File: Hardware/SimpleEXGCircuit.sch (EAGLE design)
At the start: 27 parts

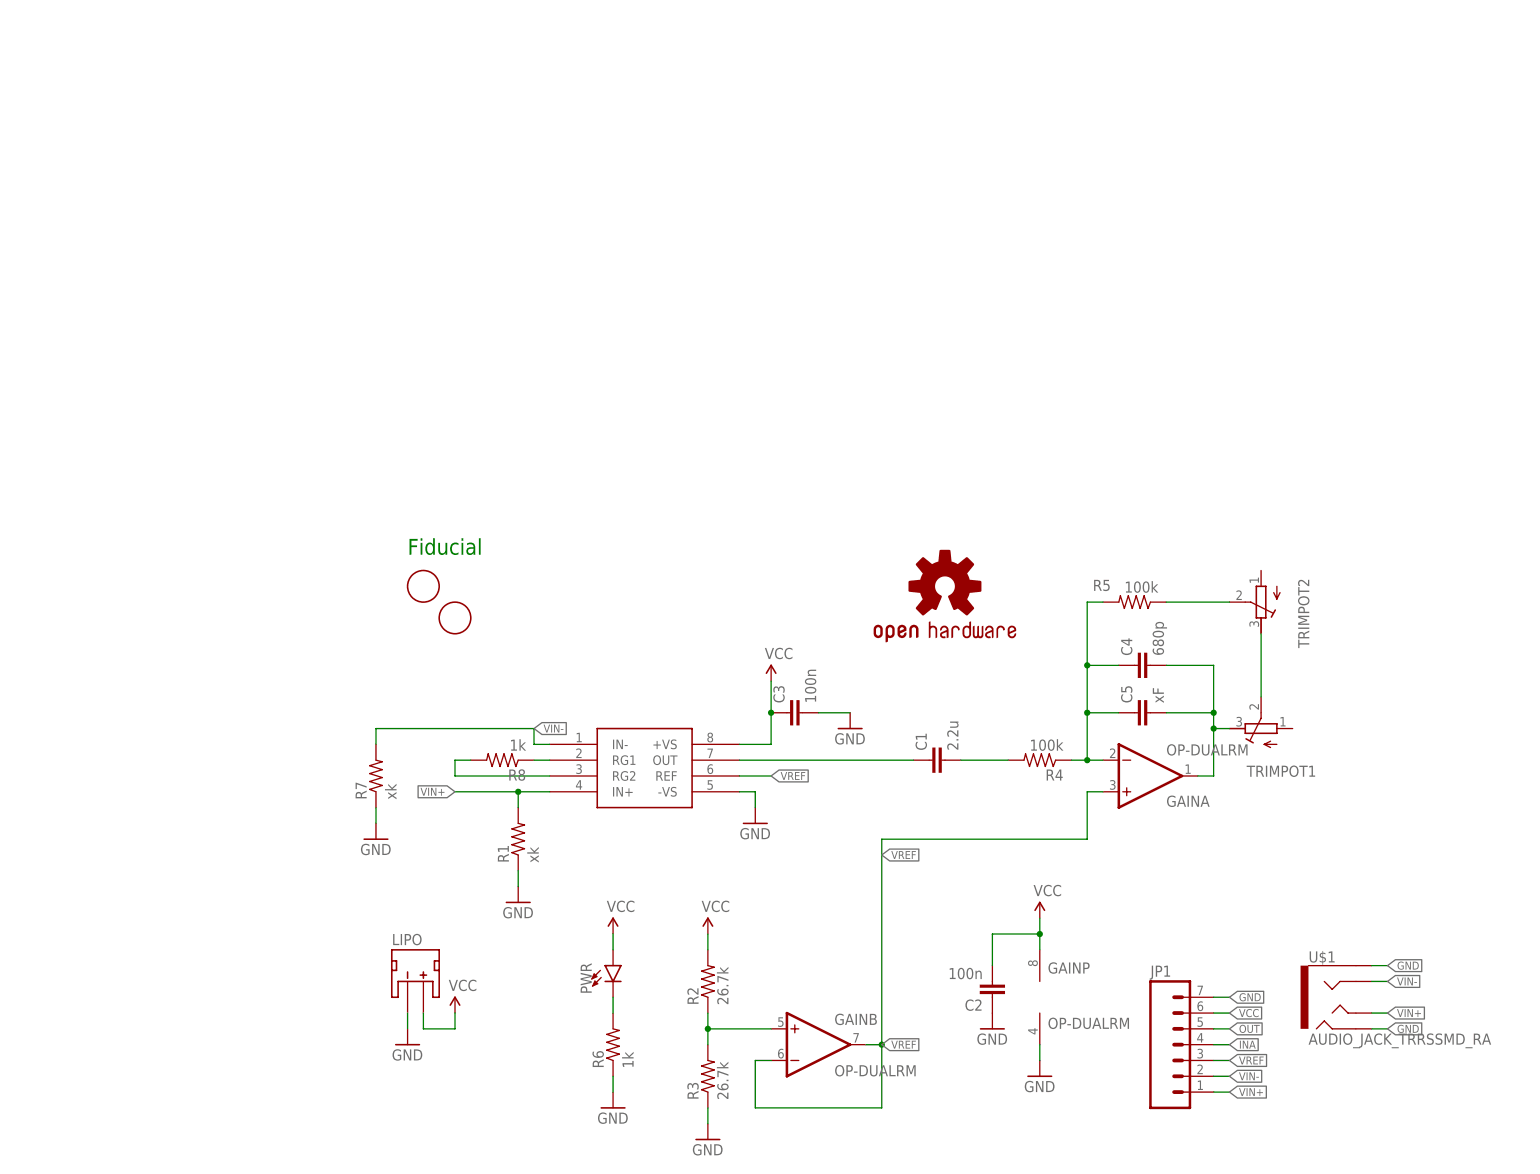
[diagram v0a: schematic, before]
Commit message: new hardware design with optoisolator and coin cell battery
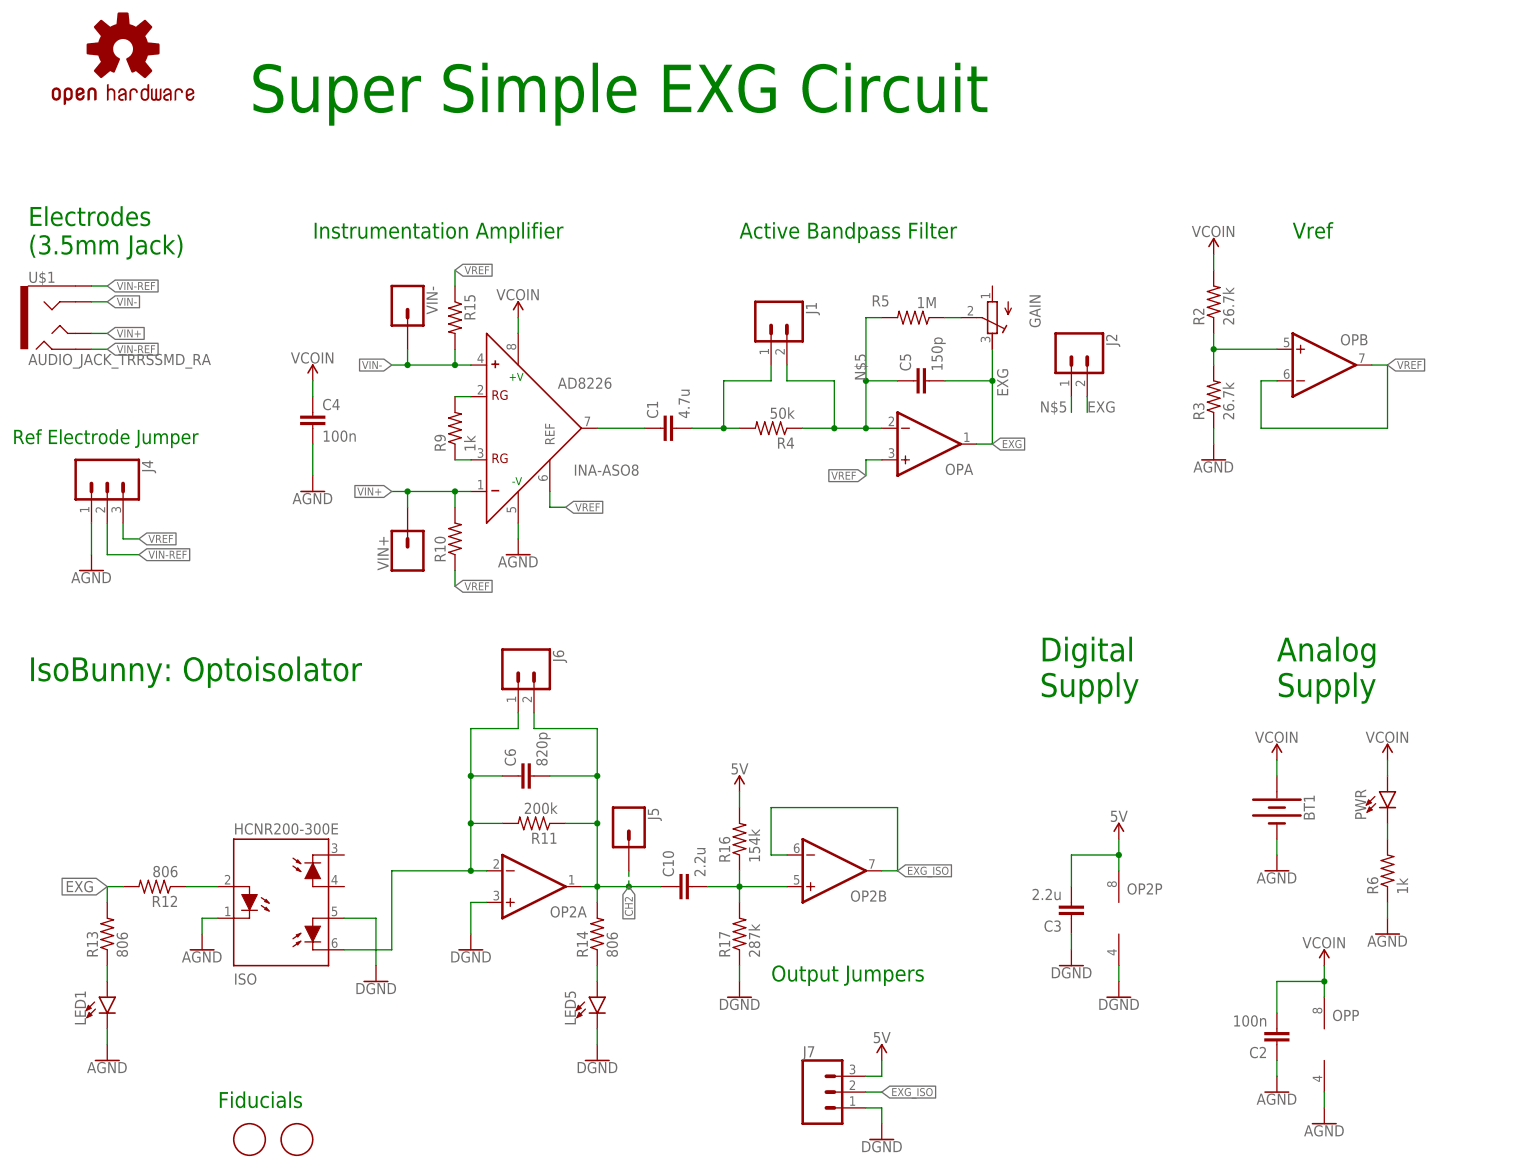
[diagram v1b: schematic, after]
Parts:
- removed INA: INA-B, CalvEngIO-AnalogIC:INA-B
- removed JP1: (no value), SparkFun-Connectors:M07
- removed LIPO: (no value), CalvEngIO-Connectors:JST_2MM_MALE
- removed R1, R7: xk, CalvEngIO-Passives:RESISTOR0402
- removed R8: 1k, CalvEngIO-Passives:RESISTOR0402
- removed TRIMPOT1, TRIMPOT2: (no value), CalvEngIO-Passives:TRIM-POT-P160
- removed U$2, U$3: FIDUCIAL, CalvEngIO-Connectors:FIDUCIAL
- added AD8226: INA-ASO8, CalvEngIO-AnalogIC:INA-ASO8
- added BT1: (no value), CalvEngIO-Connectors:BATTERY-20MM_SMD_4LEGS_OVERPASTE
- added C10: 2.2u, CalvEngIO-Passives:CAPACITOR0603
- added C6: 820p, CalvEngIO-Passives:CAPACITOR0603
- added ISO: HCNR200-300E, avago:HCNR200-300E
- added J1, J2, J6: (no value), CalvEngIO-Connectors:CONN_02
- added J4, J7: (no value), CalvEngIO-Connectors:CONN_03
- added J5: (no value), CalvEngIO-Connectors:CONN_01PTH_NO_SILK_KIT
- added LED1, LED5: (no value), CalvEngIO-LED:LED1206
- added LOGO4: OSHW-LOGOL, CalvEngIO-Logos:OSHW-LOGOL
- added OP, OP2: (no value), CalvEngIO-AnalogIC:OP-DUALR
- added R10, R15: (no value), CalvEngIO-Passives:RESISTOR0603
- added R11: 200k, CalvEngIO-Passives:RESISTOR0603
- added R12, R13, R14: 806, CalvEngIO-Passives:RESISTOR0603
- added R16: 154k, CalvEngIO-Passives:RESISTOR0603
- added R17: 287k, CalvEngIO-Passives:RESISTOR0603
- added R9: 1k, CalvEngIO-Passives:RESISTOR0603
- added VIN+, VIN-: (no value), CalvEngIO-Connectors:CONN_01
- C1: value 2.2u -> 4.7u
- C2: device CalvEngIO-Passives:CAPACITOR0402 -> CalvEngIO-Passives:CAPACITOR0603
- C3: value 100n -> 2.2u; device CalvEngIO-Passives:CAPACITOR0402 -> CalvEngIO-Passives:CAPACITOR0603
- C4: value 680p -> 100n; device CalvEngIO-Passives:CAPACITOR0402 -> CalvEngIO-Passives:CAPACITOR0603
- C5: value xF -> 150p; device resistor:C-EU025-024X044 -> CalvEngIO-Passives:CAPACITOR0603
- GAIN: value OP-DUALRM -> (none); device CalvEngIO-AnalogIC:OP-DUALRM -> CalvEngIO-Passives:TRIM-POT-P160
- LOGO1: value OSHW-LOGOS -> REVISION.C; device SparkFun-Aesthetics:OSHW-LOGOS -> CalvEngIO-Logos:REVISION.C
- PWR: device CalvEngIO-LED:LED0603 -> CalvEngIO-LED:LED1206
- R2, R3, R6: device CalvEngIO-Passives:RESISTOR0402 -> CalvEngIO-Passives:RESISTOR0603
- R4: value 100k -> 50k; device CalvEngIO-Passives:RESISTOR0402 -> CalvEngIO-Passives:RESISTOR0603
- R5: value 100k -> 1M; device CalvEngIO-Passives:RESISTOR0402 -> CalvEngIO-Passives:RESISTOR0603
- U$4: value WEBSITE.05 -> CALVENGIO_HANDLEHANDLE.05; device CalvEngIO-Logos:WEBSITE.05 -> CalvEngIO-Logos:CALVENGIO_HANDLEHANDLE.05
- U$5: value @HANDLE.1 -> FIDUCIAL; device CalvEngIO-Logos:@HANDLE.1 -> CalvEngIO-Connectors:FIDUCIAL
- U$6: value @HANDLE.05 -> FIDUCIAL; device CalvEngIO-Logos:@HANDLE.05 -> CalvEngIO-Connectors:FIDUCIAL
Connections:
- removed net GND: C2.1, C3.2, GAINP.V-, INA.-VS, JP1.7, LIPO.-, R1.1, R3.1, R6.1, R7.1, U$1.EARTH, U$1.RING2
- removed net N$4: C1.2, R4.2
- removed net OUT: C4.2, C5.2, GAINA.OUT, JP1.5, TRIMPOT1.E
- removed net VCC: C2.2, C3.1, GAINP.V+, INA.+VS, JP1.6, LIPO.+, PWR.A, R2.2
- new net 5V: C3.2, J7.3, OP2P.V+, R16.2
- new net AGND: AD8226.-V, BT1.-, C2.1, C4.2, ISO.C, J4.1, LED1.C, OPP.V-, R3.1, R6.1
- new net CH2: C10.1, C6.2, J5.1, J6.2, OP2A.OUT, R11.1, R14.2
- new net DGND: C3.1, ISO.A2, J7.1, LED5.C, OP2A.+IN, OP2P.V-, R17.1
- new net EXG: C5.2, GAIN.E, J2.2, OPA.OUT, R12.2, R13.2
- new net EXG_ISO: J7.2, OP2B.-IN, OP2B.OUT
- new net N$10: C6.1, ISO.C2, J6.1, OP2A.-IN, R11.2
- new net N$11: ISO.A, R12.1
- new net N$12: C10.2, OP2B.+IN, R16.1, R17.2
- new net N$17: LED1.A, R13.1
- new net N$19: LED5.A, R14.1
- new net VCOIN: AD8226.+V, BT1.+, C2.2, C4.1, OPP.V+, PWR.A, R2.2
- new net VIN-REF: J4.2, U$1.EARTH, U$1.RING2
- net INA: now also AD8226.OUT; no longer INA.OUT, JP1.4
- net N$1: now also GAIN.S; no longer TRIMPOT2.S
- net N$2: now also AD8226.RG@1, R9.2; no longer TRIMPOT1.S, TRIMPOT2.E
- net N$3: now also OPB.+IN; no longer GAINB.+IN
- net N$5: now also J1.2, J2.1, OPA.-IN; no longer C4.1, GAINA.-IN
- net N$7: now also AD8226.RG@2, R9.1; no longer INA.RG1, R8.1
- net N$8: now also C1.2, J1.1, R4.2; no longer INA.RG2, R8.2
- net VIN+: now also AD8226.IN-, R10.2, VIN+.1; no longer INA.IN+, JP1.1, R1.2
- net VIN-: now also AD8226.IN+, R15.2, VIN-.1; no longer INA.IN-, JP1.2, R7.2
- net VREF: now also AD8226.REF, J4.3, OPA.+IN, OPB.-IN, OPB.OUT, R10.1, R15.1; no longer GAINA.+IN, GAINB.-IN, GAINB.OUT, INA.REF, JP1.3
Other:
- note added: "Active Bandpass Filter"
- note added: "Analog Supply"
- note added: "Digital Supply"
- note added: "Electrodes (3.5mm Jack)"
- note added: "Fiducials"
- note added: "Instrumentation Amplifier"
- note added: "IsoBunny: Optoisolator"
- note added: "Output Jumpers"
- note added: "Ref Electrode Jumper"
- note added: "Super Simple EXG Circuit"
- note added: "Vref"
- note removed: "Creative Commons License Attribution-ShareAlike 4.0 Unported CC BY-SA-4.0"
- note removed: "Fiducial"
- note removed: "Super Simple EXG Circuit @OSHoilett @CalvEngIO"
- moved on the sheet: C1, C2, C3, C4, C5, PWR, R2, R3, R4, R5, R6, U$1
